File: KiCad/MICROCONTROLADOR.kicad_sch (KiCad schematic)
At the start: 18 parts, among them J3 Screw_Terminal_01x05, SW8 SW_Push, U7 MCP23017_SP, U8 PIC24HJ128GP502, Y1 8 MHz

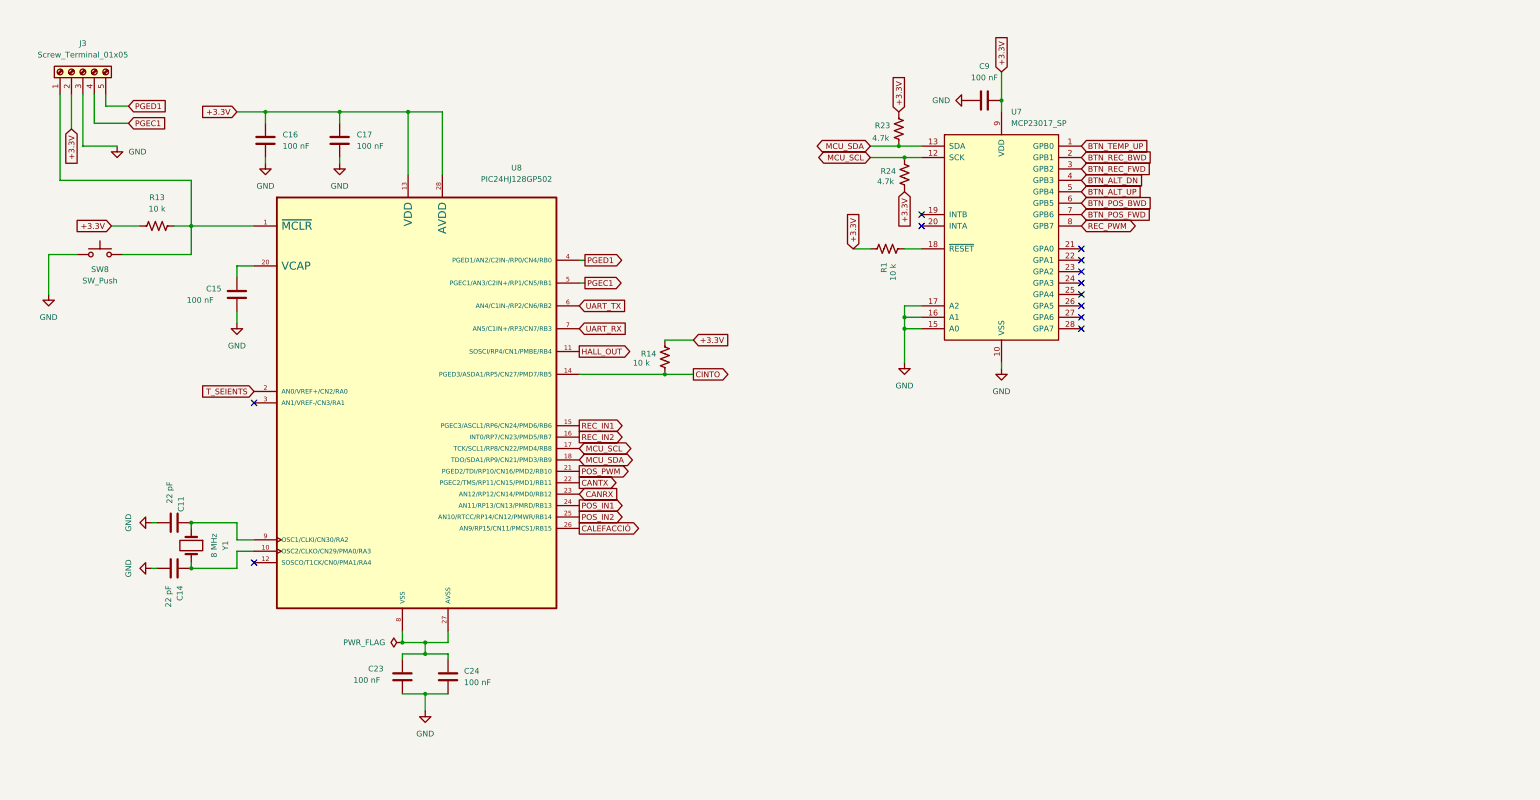
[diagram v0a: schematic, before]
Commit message: Afegit PIC 44 pins
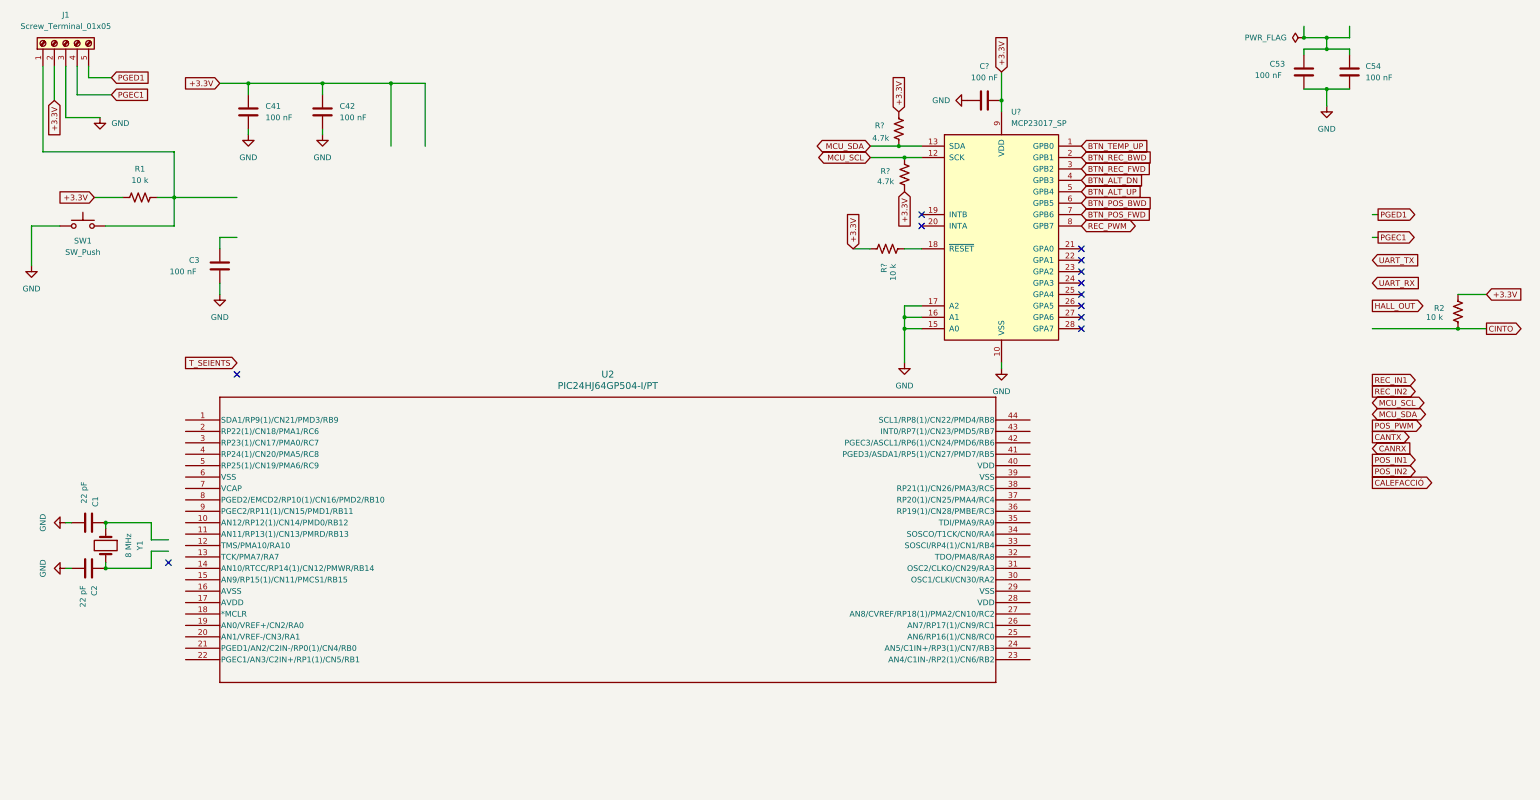
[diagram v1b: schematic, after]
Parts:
- removed U8: PIC24HJ128GP502, PIC24HJ128GP502-I_SP:DIP787W46P254L3467H508Q28, symbol PIC24HJ128GP502-I_SP:PIC24HJ128GP502-I_SP
- added U2: PIC24HJ64GP504-I/PT, TQFP44_10x10MC_MCH, symbol MICRO:PIC24HJ64GP504-I_PT
- renumbered C11 to C1, C14 to C2, C15 to C3, C16 to C41, C17 to C42, C23 to C53, C24 to C54, C9 to C?, J3 to J1, R13 to R1, R14 to R2, R23 to R?, R24 to R?, R1 to R?, SW8 to SW1, U7 to U?
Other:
- moved on the sheet: C1, C2, C3, C41, C42, C53, C54, J1, R1, R2, SW1, Y1

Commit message: Micro editat simbol
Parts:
- removed C?: 100 nF, Capacitor_SMD:C_0805_2012Metric, symbol Device:C
- removed R2, R?: 10 k, Resistor_SMD:R_0805_2012Metric, symbol Device:R_US
- removed U?: MCP23017_SP, Package_DIP:DIP-28_W7.62mm, symbol Interface_Expansion:MCP23017_SP
- U2: footprint TQFP44_10x10MC_MCH -> MICRO:TQFP44_10x10MC_MCH-L
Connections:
- no-connect marks 12 -> 2
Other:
- moved on the sheet: U2

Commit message: NOTAS
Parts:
- removed R? (x2): 4.7k, Resistor_SMD:R_0805_2012Metric, symbol Device:R_US
- added C4, C5: 100 nF, Capacitor_SMD:C_0805_2012Metric, symbol Device:C
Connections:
- net GND: now also C4.2, C5.2
- net at C2.1, Y1.2: now also U2.31 (OSC2/CLKO/CN29/RA3)
- net at C53.1, C54.1: now also U2.29 (VSS), U2.40 (VDD)
- net at U2.28 (VDD): now also U2.39 (VSS), C4.1, C5.1
- net at U2.30 (OSC1/CLKI/CN30/RA2): now also C1.1, Y1.1
- no-connect marks 2 -> 0
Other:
- moved on the sheet: C1, C2, C53, C54, U2, Y1

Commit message: Modificat el placement
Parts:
- added C6, C7: 100 nF, Capacitor_SMD:C_0805_2012Metric, symbol Device:C
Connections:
- net +3.3V: now also U2.17 (AVDD), U2.7 (VCAP)
- net GND: now also C6.2, C7.2
- net MCU_SCL: now also U2.44 (SCL1/RP8(1)/CN22/PMD4/RB8)
- net MCU_SDA: now also U2.1 (SDA1/RP9(1)/CN21/PMD3/RB9)
- net PGEC1: now also U2.22 (PGEC1/AN3/C2IN+/RP1(1)/CN5/RB1)
- net PGED1: now also U2.21 (PGED1/AN2/C2IN-/RP0(1)/CN4/RB0)
- net REC_IN1: now also U2.42 (PGEC3/ASCL1/RP6(1)/CN24/PMD6/RB6)
- net REC_IN2: now also U2.43 (INT0/RP7(1)/CN23/PMD5/RB7)
- net at U2.16 (AVSS): now also U2.6 (VSS), C6.1, C7.1
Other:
- moved on the sheet: C1, C2, C4, C41, C42, C5, C53, C54, U2, Y1

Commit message: Modificat el placement
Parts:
- added TP1: TestPoint, symbol Connector:TestPoint
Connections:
- net at J1.1 (Pin_1), R1.2, SW1.2: now also U2.18 (*MCLR)
- net at C2.1, U2.31 (OSC2/CLKO/CN29/RA3), Y1.2: now also TP1.1
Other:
- moved on the sheet: C3, C6, C7, J1, R1, SW1

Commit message: Modificat el placement
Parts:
- added R2: 10 k, Resistor_SMD:R_0805_2012Metric, symbol Device:R_US
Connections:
- net +3.3V: now also R2.2; no longer U2.7 (VCAP)
- net CALEFACCIÓ: now also U2.15 (AN9/RP15(1)/CN11/PMCS1/RB15)
- net CINTO: now also U2.41 (PGED3/ASDA1/RP5(1)/CN27/PMD7/RB5), R2.1
- net HALL_OUT: now also U2.33 (SOSCI/RP4(1)/CN1/RB4)
- net T_SEIENTS: now also U2.19 (AN0/VREF+/CN2/RA0)
- net UART_RX: now also U2.24 (AN5/C1IN+/RP3(1)/CN7/RB3)
- net UART_TX: now also U2.23 (AN4/C1IN-/RP2(1)/CN6/RB2)
- net at C3.1: now also U2.7 (VCAP)
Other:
- moved on the sheet: C3, C41, C42, J1, R1, SW1

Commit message: Modificat ETIQUETES MICROCONTROLADOR
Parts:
- renumbered C1 to C11, C2 to C14, C3 to C15, C41 to C16, C42 to C17, C53 to C23, C54 to C24, C7 to C70, C6 to C71, C4 to C72, C5 to C73, J1 to J3, R2 to R100, R1 to R13, SW1 to SW8, TP1 to TP10, U2 to U9
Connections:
- net CANRX: now also U9.10 (AN12/RP12(1)/CN14/PMD0/RB12)
- net CANTX: now also U9.9 (PGEC2/RP11(1)/CN15/PMD1/RB11)
- net POS_IN1: now also U9.11 (AN11/RP13(1)/CN13/PMRD/RB13)
- net POS_IN2: now also U9.14 (AN10/RTCC/RP14(1)/CN12/PMWR/RB14)
- net POS_PWM: now also U9.8 (PGED2/EMCD2/RP10(1)/CN16/PMD2/RB10)
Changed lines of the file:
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@@
 	(global_label "MCU_SDA"
 		(shape bidirectional)
-		(at 50.8 38.1 180)
+		(at 71.12 38.1 180)
 		(fields_autoplaced yes)
 		(effects
@@
 		)
 		(property "Intersheetrefs" "${INTERSHEET_REFS}"
-			(at 38.1159 38.1 0)
+			(at 58.4359 38.1 0)
 			(effects
 				(font
@@
 	(global_label "POS_PWM"
 		(shape output)
-		(at 50.8 40.64 180)
+		(at 100.33 86.36 180)
 		(fields_autoplaced yes)
 		(effects
@@
 		)
 		(property "Intersheetrefs" "${INTERSHEET_REFS}"
-			(at 38.8644 40.64 0)
+			(at 88.3944 86.36 0)
 			(effects
 				(font
@@
 	(global_label "CANRX"
 		(shape input)
-		(at 50.8 45.72 180)
+		(at 100.33 91.44 180)
 		(fields_autoplaced yes)
 		(effects
@@
 		)
 		(property "Intersheetrefs" "${INTERSHEET_REFS}"
-			(at 41.6462 45.72 0)
+			(at 91.1762 91.44 0)
 			(effects
 				(font
@@
 	(global_label "CANTX"
 		(shape output)
-		(at 50.8 43.18 180)
+		(at 100.33 88.9 180)
 		(fields_autoplaced yes)
 		(effects
@@
 		)
 		(property "Intersheetrefs" "${INTERSHEET_REFS}"
-			(at 41.9486 43.18 0)
+			(at 91.4786 88.9 0)
 			(effects
 				(font
@@
 	(global_label "POS_IN2"
 		(shape output)
-		(at 50.8 50.8 180)
+		(at 100.33 101.6 180)
 		(fields_autoplaced yes)
 		(effects
@@
 		)
 		(property "Intersheetrefs" "${INTERSHEET_REFS}"
-			(at 39.8924 50.8 0)
+			(at 89.4224 101.6 0)
 			(effects
 				(font
@@
 	(global_label "POS_IN1"
 		(shape output)
-		(at 50.8 48.26 180)
+		(at 100.33 93.98 180)
 		(fields_autoplaced yes)
 		(effects
@@
 		)
 		(property "Intersheetrefs" "${INTERSHEET_REFS}"
-			(at 39.8924 48.26 0)
+			(at 89.4224 93.98 0)
 			(effects
 				(font
@@
 	(global_label "MCU_SCL"
 		(shape bidirectional)
-		(at 50.8 35.56 180)
+		(at 71.12 35.56 180)
 		(fields_autoplaced yes)
 		(effects
@@
 		)
 		(property "Intersheetrefs" "${INTERSHEET_REFS}"
-			(at 38.1764 35.56 0)
+			(at 58.4964 35.56 0)
 			(effects
 				(font
@@
 		(dnp no)
 		(fields_autoplaced yes)
-		(property "Reference" "J1"
+		(property "Reference" "J3"
 			(at 55.88 68.58 90)
 			(effects
@@
 		(on_board yes)
 		(dnp no)
-		(property "Reference" "C2"
+		(property "Reference" "C14"
 			(at 217.932 46.736 90)
 			(effects
@@
 		(dnp no)
 		(fields_autoplaced yes)
-		(property "Reference" "TP1"
+		(property "Reference" "TP10"
 			(at 209.55 46.2279 0)
 			(effects
@@
 				)
 			)
+			(project "SEIENTS_EDD"
+				(path "/b6401b4f-5426-49b8-bb2e-8ecdb19989ef/2352108e-71c7-4bd2-90ee-aa6ba1d65197"
+					(reference "TP10")
+					(unit 1)
+				)
+			)
 		)
 	)
@@
 		(dnp no)
 		(fields_autoplaced yes)
-		(property "Reference" "R1"
+		(property "Reference" "R13"
 			(at 72.39 102.87 90)
 			(effects
@@
 		(dnp no)
 		(fields_autoplaced yes)
-		(property "Reference" "#PWR010"
+		(property "Reference" "#PWR?"
 			(at 162.56 15.24 0)
 			(effects
@@
 				)
 			)
+			(project "SEIENTS_EDD"
+				(path "/b6401b4f-5426-49b8-bb2e-8ecdb19989ef/2352108e-71c7-4bd2-90ee-aa6ba1d65197"
+					(reference "#PWR?")
+					(unit 1)
+				)
+			)
 		)
 	)
@@
 		(dnp no)
 		(fields_autoplaced yes)
-		(property "Reference" "#PWR05"
+		(property "Reference" "#PWR023"
 			(at 63.5 97.79 0)
 			(effects
@@
 		(on_board yes)
 		(dnp no)
-		(property "Reference" "C54"
+		(property "Reference" "C24"
 			(at 148.336 161.29 0)
 			(effects
@@
 		(dnp no)
 		(fields_autoplaced yes)
-		(property "Reference" "C41"
+		(property "Reference" "C16"
 			(at 114.3 35.5599 0)
 			(effects
@@
 		(dnp no)
 		(fields_autoplaced yes)
-		(property "Reference" "#PWR04"
+		(property "Reference" "#PWR034"
 			(at 127 48.26 0)
 			(effects
@@
 		(on_board yes)
 		(dnp no)
-		(property "Reference" "C6"
+		(property "Reference" "C71"
 			(at 173.736 25.654 0)
 			(effects
@@
 				)
 			)
+			(project "SEIENTS_EDD"
+				(path "/b6401b4f-5426-49b8-bb2e-8ecdb19989ef/2352108e-71c7-4bd2-90ee-aa6ba1d65197"
+					(reference "C71")
+					(unit 1)
+				)
+			)
 		)
 	)
@@
 		(dnp no)
 		(fields_autoplaced yes)
-		(property "Reference" "#PWR08"
+		(property "Reference" "#PWR037"
 			(at 140.97 171.45 0)
 			(effects
@@
 		(on_board yes)
 		(dnp no)
-		(property "Reference" "C5"
+		(property "Reference" "C73"
 			(at 173.736 156.21 0)
 			(effects
@@
 				)
 			)
+			(project "SEIENTS_EDD"
+				(path "/b6401b4f-5426-49b8-bb2e-8ecdb19989ef/2352108e-71c7-4bd2-90ee-aa6ba1d65197"
+					(reference "C73")
+					(unit 1)
+				)
+			)
 		)
 	)
@@
 		(dnp no)
 		(fields_autoplaced yes)
-		(property "Reference" "#FLG02"
+		(property "Reference" "#FLG?"
 			(at 170.815 36.83 0)
 			(effects
@@
 				)
 			)
+			(project "SEIENTS_EDD"
+				(path "/b6401b4f-5426-49b8-bb2e-8ecdb19989ef/2352108e-71c7-4bd2-90ee-aa6ba1d65197"
+					(reference "#FLG?")
+					(unit 1)
+				)
+			)
 		)
 	)
@@
 		(dnp no)
 		(fields_autoplaced yes)
-		(property "Reference" "R2"
+		(property "Reference" "R100"
 			(at 238.76 69.8499 0)
 			(effects
@@
 				)
 			)
+			(project "SEIENTS_EDD"
+				(path "/b6401b4f-5426-49b8-bb2e-8ecdb19989ef/2352108e-71c7-4bd2-90ee-aa6ba1d65197"
+					(reference "R100")
+					(unit 1)
+				)
+			)
 		)
 	)
@@
 		(dnp no)
 		(fields_autoplaced yes)
-		(property "Reference" "#PWR02"
+		(property "Reference" "#PWR025"
 			(at 227.33 50.8 0)
 			(effects
@@
 		(on_board yes)
 		(dnp no)
-		(property "Reference" "C7"
+		(property "Reference" "C70"
 			(at 155.194 25.4 0)
 			(effects
@@
 				)
 			)
+			(project "SEIENTS_EDD"
+				(path "/b6401b4f-5426-49b8-bb2e-8ecdb19989ef/2352108e-71c7-4bd2-90ee-aa6ba1d65197"
+					(reference "C70")
+					(unit 1)
+				)
+			)
 		)
 	)
@@
 		(dnp no)
 		(fields_autoplaced yes)
-		(property "Reference" "#PWR09"
+		(property "Reference" "#PWR?"
 			(at 165.1 171.45 0)
 			(effects
@@
 				)
 			)
+			(project "SEIENTS_EDD"
+				(path "/b6401b4f-5426-49b8-bb2e-8ecdb19989ef/2352108e-71c7-4bd2-90ee-aa6ba1d65197"
+					(reference "#PWR?")
+					(unit 1)
+				)
+			)
 		)
 	)
@@
 		(dnp no)
 		(fields_autoplaced yes)
-		(property "Reference" "U2"
-			(at 151.892 59.436 0)
+		(property "Reference" "U9"
+			(at 169.7833 44.45 0)
 			(effects
 				(font
 					(size 1.524 1.524)
 				)
+				(justify left)
 			)
 		)
 		(property "Value" "PIC24HJ64GP504-I/PT"
-			(at 151.892 61.976 0)
+			(at 169.7833 46.99 0)
 			(effects
 				(font
 					(size 1.524 1.524)
 				)
+				(justify left)
 			)
 		)
@@
 				)
 			)
+			(project "SEIENTS_EDD"
+				(path "/b6401b4f-5426-49b8-bb2e-8ecdb19989ef/2352108e-71c7-4bd2-90ee-aa6ba1d65197"
+					(reference "U9")
+					(unit 1)
+				)
+			)
 		)
 	)
@@
 		(on_board yes)
 		(dnp no)
-		(property "Reference" "#FLG03"
+		(property "Reference" "#FLG01"
 			(at 133.985 149.86 0)
 			(effects
@@
 		(dnp no)
 		(fields_autoplaced yes)
-		(property "Reference" "#PWR06"
+		(property "Reference" "#PWR022"
 			(at 48.26 130.81 0)
 			(effects
@@
 		(on_board yes)
 		(dnp no)
-		(property "Reference" "C53"
+		(property "Reference" "C23"
 			(at 128.27 155.702 0)
 			(effects
@@
 		(on_board yes)
 		(dnp no)
-		(property "Reference" "C3"
+		(property "Reference" "C15"
 			(at 142.24 27.94 0)
 			(effects
@@
 		(dnp no)
 		(fields_autoplaced yes)
-		(property "Reference" "#PWR03"
+		(property "Reference" "#PWR033"
 			(at 110.49 48.26 0)
 			(effects
@@
 		(dnp no)
 		(fields_autoplaced yes)
-		(property "Reference" "#PWR07"
+		(property "Reference" "#PWR?"
 			(at 128.27 26.67 0)
 			(effects
@@
 				)
 			)
+			(project "SEIENTS_EDD"
+				(path "/b6401b4f-5426-49b8-bb2e-8ecdb19989ef/2352108e-71c7-4bd2-90ee-aa6ba1d65197"
+					(reference "#PWR?")
+					(unit 1)
+				)
+			)
 		)
 	)
@@
 		(on_board yes)
 		(dnp no)
-		(property "Reference" "SW1"
+		(property "Reference" "SW8"
 			(at 59.69 118.872 0)
 			(effects
@@
 		(dnp no)
 		(fields_autoplaced yes)
-		(property "Reference" "C42"
+		(property "Reference" "C17"
 			(at 130.81 35.5599 0)
 			(effects
@@
 		(on_board yes)
 		(dnp no)
-		(property "Reference" "C4"
+		(property "Reference" "C72"
 			(at 155.194 152.654 0)
 			(effects
@@
 				)
 			)
+			(project "SEIENTS_EDD"
+				(path "/b6401b4f-5426-49b8-bb2e-8ecdb19989ef/2352108e-71c7-4bd2-90ee-aa6ba1d65197"
+					(reference "C72")
+					(unit 1)
+				)
+			)
 		)
 	)
@@
 		(dnp no)
 		(fields_autoplaced yes)
-		(property "Reference" "#PWR01"
+		(property "Reference" "#PWR024"
 			(at 227.33 60.96 0)
 			(effects
@@
 		(on_board yes)
 		(dnp no)
-		(property "Reference" "#FLG01"
+		(property "Reference" "#FLG?"
 			(at 172.085 149.86 0)
 			(effects
@@
 				)
 			)
+			(project "SEIENTS_EDD"
+				(path "/b6401b4f-5426-49b8-bb2e-8ecdb19989ef/2352108e-71c7-4bd2-90ee-aa6ba1d65197"
+					(reference "#FLG?")
+					(unit 1)
+				)
+			)
 		)
 	)
@@
 		(on_board yes)
 		(dnp no)
-		(property "Reference" "C1"
+		(property "Reference" "C11"
 			(at 220.472 66.548 90)
 			(effects

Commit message: Modificat ETIQUETES MICROCONTROLADOR i errors varis
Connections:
- no-connect marks 0 -> 16
